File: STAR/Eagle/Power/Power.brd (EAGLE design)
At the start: 51 x 40.4 mm, 51 parts, among them J1 J30J-25, U1 LMR16020, U2 LMR16020, U3 LMR16020

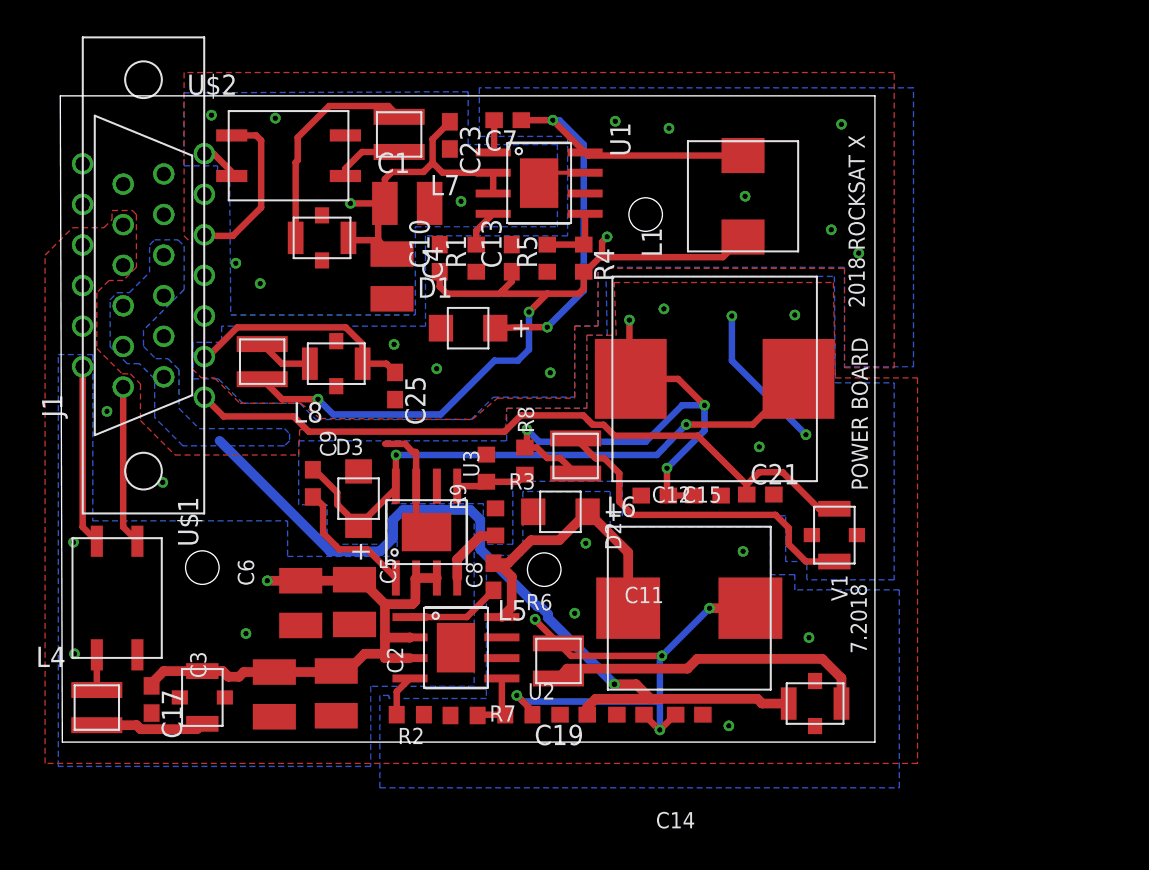
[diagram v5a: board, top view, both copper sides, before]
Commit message: Fixed Blaire's  nonsense on the power board. No longer shorting 3V3 to GSE_GND. The input names still make no sense
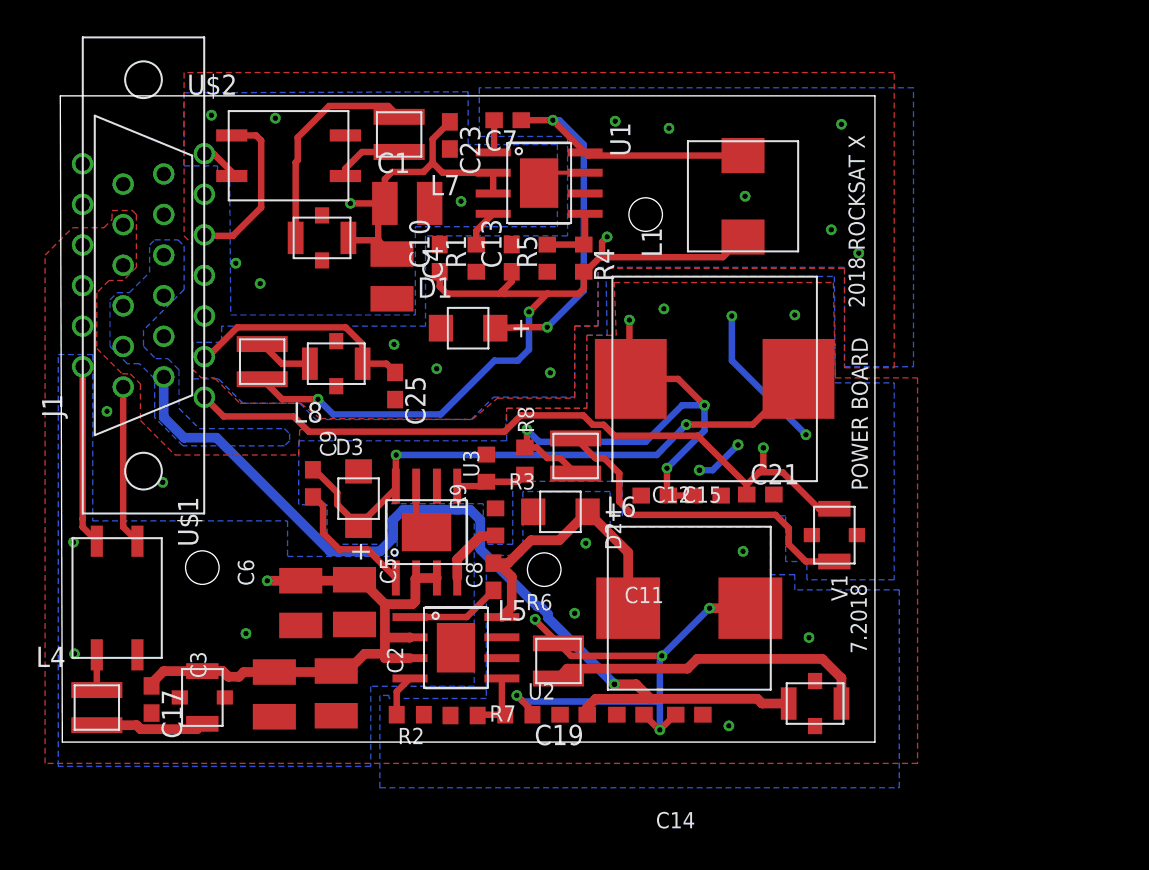
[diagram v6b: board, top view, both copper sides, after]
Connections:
- net EW renamed H
- net N$40 renamed L
- net N$42 renamed K
- net N$43 renamed J
- net N$44 renamed I
- net GSE_GND: now also U$4.P$4, U$4.P$5
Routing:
- net 5V_FILT: track 51.1 -> 57.8 mm
- net GSE_GND: track 16.8 -> 15.6 mm, vias 7 -> 8
- net 3V3_FILT: track 44.9 -> 46.1 mm, vias 0 -> 1
- net GSE_UFILT: track 11.9 -> 11.3 mm
- added copper zone on layer 16, net 3V3_FILT
- removed copper zone on layer 16, net GSE_GND
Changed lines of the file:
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@@
 <?xml version="1.0" encoding="utf-8"?>
 <!DOCTYPE eagle SYSTEM "eagle.dtd">
-<eagle version="7.6.0">
+<eagle version="9.1.0">
 <drawing>
 <settings>
 <setting alwaysvectorfont="no"/>
+<setting keepoldvectorfont="yes"/>
 <setting verticaltext="up"/>
 </settings>
@@
 <param name="dpMaxLengthDifference" value="10mm"/>
 <param name="dpGapFactor" value="2.5"/>
-<param name="checkGrid" value="0"/>
 <param name="checkAngle" value="0"/>
 <param name="checkFont" value="1"/>
 <param name="checkRestrict" value="1"/>
+<param name="checkStop" value="0"/>
+<param name="checkValues" value="0"/>
+<param name="checkNames" value="1"/>
+<param name="checkWireStubs" value="1"/>
+<param name="checkPolygonWidth" value="0"/>
 <param name="useDiameter" value="13"/>
 <param name="maxErrors" value="50"/>
@@
 <contactref element="U$1" pad="P$2"/>
 <contactref element="J1" pad="15"/>
-<wire x1="-4.191" y1="6.223" x2="-4.191" y2="5.588" width="0.4064" layer="1"/>
-<wire x1="-5.08" y1="17.145" x2="-5.08" y2="7.112" width="0.4064" layer="1"/>
-<wire x1="-5.08" y1="7.112" x2="-4.191" y2="6.223" width="0.4064" layer="1"/>
+<wire x1="-5.08" y1="17.145" x2="-5.08" y2="7.62" width="0.4064" layer="1"/>
+<wire x1="-5.08" y1="7.112" x2="-5.08" y2="7.62" width="0.4064" layer="1"/>
+<wire x1="-4.191" y1="6.223" x2="-5.08" y2="7.112" width="0.4064" layer="1"/>
 </signal>
 <signal name="GSE_FILT">
@@
 <wire x1="14.351" y1="6.4135" x2="13.5255" y2="5.588" width="0.6096" layer="16"/>
 <wire x1="13.5255" y1="5.588" x2="10.414" y2="5.588" width="0.6096" layer="16"/>
-<wire x1="10.414" y1="5.588" x2="3.4925" y2="12.5095" width="0.6096" layer="16"/>
 <wire x1="19.812" y1="5.715" x2="19.812" y2="7.5565" width="0.6096" layer="16"/>
 <via x="28.2054875" y="-2.7305" extent="1-16" drill="0.35"/>
 <wire x1="28.2054875" y1="-2.7305" x2="29.5656" y2="-2.7305" width="0.6096" layer="1"/>
 <wire x1="29.5656" y1="-2.7305" x2="30.48" y2="-3.6449" width="0.6096" layer="1"/>
+<wire x1="3.302" y1="12.7" x2="1.27" y2="12.7" width="0.6096" layer="16"/>
+<wire x1="1.27" y1="12.7" x2="0" y2="13.97" width="0.6096" layer="16"/>
+<wire x1="0" y1="13.97" x2="0" y2="16.51" width="0.6096" layer="16"/>
+<wire x1="10.414" y1="5.588" x2="3.302" y2="12.7" width="0.6096" layer="16"/>
 </signal>
 <signal name="3V3_FILT">
@@
 <wire x1="3.7465" y1="14.0335" x2="2.54" y2="15.24" width="0.4064" layer="1"/>
 <wire x1="22.352" y1="14.097" x2="26.26360625" y2="14.097" width="0.4064" layer="1"/>
-<wire x1="26.26360625" y1="14.097" x2="26.530303125" y2="13.830303125" width="0.4064" layer="1"/>
-<wire x1="26.530303125" y1="13.830303125" x2="26.83320625" y2="13.5274" width="0.4064" layer="1"/>
 <wire x1="33.4155" y1="12.827" x2="36.488" y2="9.7545" width="0.4064" layer="1"/>
-<wire x1="26.530303125" y1="13.830303125" x2="26.84800625" y2="13.5126" width="0.4064" layer="1"/>
-<wire x1="26.84800625" y1="13.5126" x2="27.52829375" y2="13.5126" width="0.4064" layer="1"/>
 <wire x1="27.52829375" y1="13.5126" x2="28.21389375" y2="12.827" width="0.4064" layer="1"/>
 <wire x1="28.21389375" y1="12.827" x2="33.4155" y2="12.827" width="0.4064" layer="1"/>
+<polygon width="0.4064" layer="16">
+<vertex x="45.72" y="3.81"/>
+<vertex x="40.259" y="3.81"/>
+<vertex x="40.259" y="4.953"/>
+<vertex x="38.9255" y="4.953"/>
+<vertex x="38.9255" y="7.8105"/>
+<vertex x="28.702" y="7.8105"/>
+<vertex x="28.702" y="9.9695"/>
+<vertex x="21.844" y="9.9695"/>
+<vertex x="21.844" y="6.0325"/>
+<vertex x="20.0025" y="6.0325"/>
+<vertex x="20.0025" y="8.5725"/>
+<vertex x="13.97" y="8.5725"/>
+<vertex x="13.97" y="6.0325"/>
+<vertex x="10.2235" y="6.0325"/>
+<vertex x="10.2235" y="8.509"/>
+<vertex x="8.4455" y="8.509"/>
+<vertex x="8.4455" y="12.5095"/>
+<vertex x="21.463" y="12.5095"/>
+<vertex x="21.463" y="14.5415"/>
+<vertex x="26.4795" y="14.5415"/>
+<vertex x="26.4795" y="19.1135"/>
+<vertex x="27.7495" y="19.1135"/>
+<vertex x="27.686" y="22.7965"/>
+<vertex x="41.9735" y="22.7965"/>
+<vertex x="42.037" y="16.129"/>
+<vertex x="45.72" y="16.129"/>
+</polygon>
+<via x="37.5285" y="12.065" extent="1-16" drill="0.35"/>
+<wire x1="37.5285" y1="12.065" x2="37.5285" y2="10.795" width="0.4064" layer="1"/>
+<wire x1="37.5285" y1="10.795" x2="37.2745" y2="10.541" width="0.4064" layer="1"/>
+<wire x1="26.26360625" y1="14.097" x2="26.84800625" y2="13.5126" width="0.4064" layer="1"/>
+<wire x1="26.84800625" y1="13.5126" x2="27.52829375" y2="13.5126" width="0.4064" layer="1"/>
 </signal>
 <signal name="N$29">
@@
 <wire x1="16.4465" y1="6.7945" x2="15.7965" y2="7.4445" width="0.4064" layer="1"/>
 <wire x1="15.7965" y1="7.4445" x2="15.7965" y2="9.6695" width="0.4064" layer="1"/>
-<wire x1="13.8557" y1="12.319" x2="15.113" y2="12.319" width="0.4064" layer="1"/>
-<wire x1="15.113" y1="12.319" x2="15.5575" y2="11.811" width="0.4064" layer="1"/>
-<wire x1="15.5575" y1="11.811" x2="15.748" y2="11.811" width="0.4064" layer="1"/>
-<wire x1="15.748" y1="11.811" x2="15.7965" y2="11.7625" width="0.4064" layer="1"/>
-<wire x1="15.7965" y1="11.7625" x2="15.7965" y2="9.6695" width="0.4064" layer="1"/>
 <contactref element="C6" pad="2"/>
 <contactref element="C3" pad="2"/>
@@
 <wire x1="35.56" y1="17.526" x2="40.1955" y2="12.8905" width="0.4064" layer="16"/>
 <via x="39.497" y="20.3835" extent="1-16" drill="0.3302" diameter="0.3302"/>
-<via x="37.2745" y="12.1285" extent="1-16" drill="0.3302" diameter="0.3302"/>
-<polygon width="0.4064" layer="16">
-<vertex x="45.72" y="3.81"/>
-<vertex x="40.259" y="3.81"/>
-<vertex x="40.259" y="4.953"/>
-<vertex x="38.9255" y="4.953"/>
-<vertex x="38.9255" y="7.8105"/>
-<vertex x="28.702" y="7.8105"/>
-<vertex x="28.702" y="9.9695"/>
-<vertex x="21.844" y="9.9695"/>
-<vertex x="21.844" y="6.0325"/>
-<vertex x="20.0025" y="6.0325"/>
-<vertex x="20.0025" y="8.5725"/>
-<vertex x="13.97" y="8.5725"/>
-<vertex x="13.97" y="6.0325"/>
-<vertex x="10.2235" y="6.0325"/>
-<vertex x="10.2235" y="8.509"/>
-<vertex x="8.4455" y="8.509"/>
-<vertex x="8.4455" y="12.5095"/>
-<vertex x="21.463" y="12.5095"/>
-<vertex x="21.463" y="14.5415"/>
-<vertex x="26.4795" y="14.5415"/>
-<vertex x="26.4795" y="19.1135"/>
-<vertex x="27.7495" y="19.1135"/>
-<vertex x="27.686" y="22.7965"/>
-<vertex x="41.9735" y="22.7965"/>
-<vertex x="42.037" y="16.129"/>
-<vertex x="45.72" y="16.129"/>
-</polygon>
-<wire x1="34.886" y1="9.0805" x2="38.188" y2="9.144" width="0" layer="19" extent="1-1"/>
+<contactref element="U$4" pad="P$4"/>
+<contactref element="U$4" pad="P$5"/>
+<via x="33.528" y="10.668" extent="1-16" drill="0.35"/>
+<via x="35.941" y="12.2555" extent="1-16" drill="0.35"/>
+<wire x1="33.528" y1="10.668" x2="34.3535" y2="10.668" width="0.4064" layer="16"/>
+<wire x1="34.3535" y1="10.668" x2="35.941" y2="12.2555" width="0.4064" layer="16"/>
 </signal>
 <signal name="TE_UFILT">
@@
 <contactref element="J1" pad="13"/>
 <wire x1="2.54" y1="30.48" x2="3.1115" y2="30.48" width="0.4064" layer="1"/>
-<wire x1="4.2545" y1="29.337" x2="3.1115" y2="30.48" width="0.4064" layer="1"/>
-<wire x1="4.2545" y1="29.337" x2="4.2545" y2="29.083" width="0" layer="19" extent="1-1"/>
-</signal>
-<signal name="N$40">
+<wire x1="3.1115" y1="30.48" x2="4.2545" y2="29.337" width="0.4064" layer="1"/>
+<wire x1="4.2545" y1="29.337" x2="4.2545" y2="29.083" width="0.4064" layer="1"/>
+</signal>
+<signal name="L">
 <contactref element="J1" pad="11"/>
 </signal>
-<signal name="N$42">
+<signal name="K">
 <contactref element="J1" pad="25"/>
 </signal>
-<signal name="N$43">
+<signal name="J">
 <contactref element="J1" pad="24"/>
 </signal>
-<signal name="N$44">
+<signal name="I">
 <contactref element="J1" pad="23"/>
 </signal>
@@
 <contactref element="J1" pad="10"/>
 </signal>
-<signal name="EW">
+<signal name="H">
 <contactref element="J1" pad="12"/>
 </signal>
 </signals>
+<mfgpreviewcolors>
+<mfgpreviewcolor name="soldermaskcolor" color="0xC8008000"/>
+<mfgpreviewcolor name="silkscreencolor" color="0xFFFEFEFE"/>
+<mfgpreviewcolor name="backgroundcolor" color="0xFF282828"/>
+<mfgpreviewcolor name="coppercolor" color="0xFFFFBF00"/>
+<mfgpreviewcolor name="substratecolor" color="0xFF786E46"/>
+</mfgpreviewcolors>
 </board>
 </drawing>

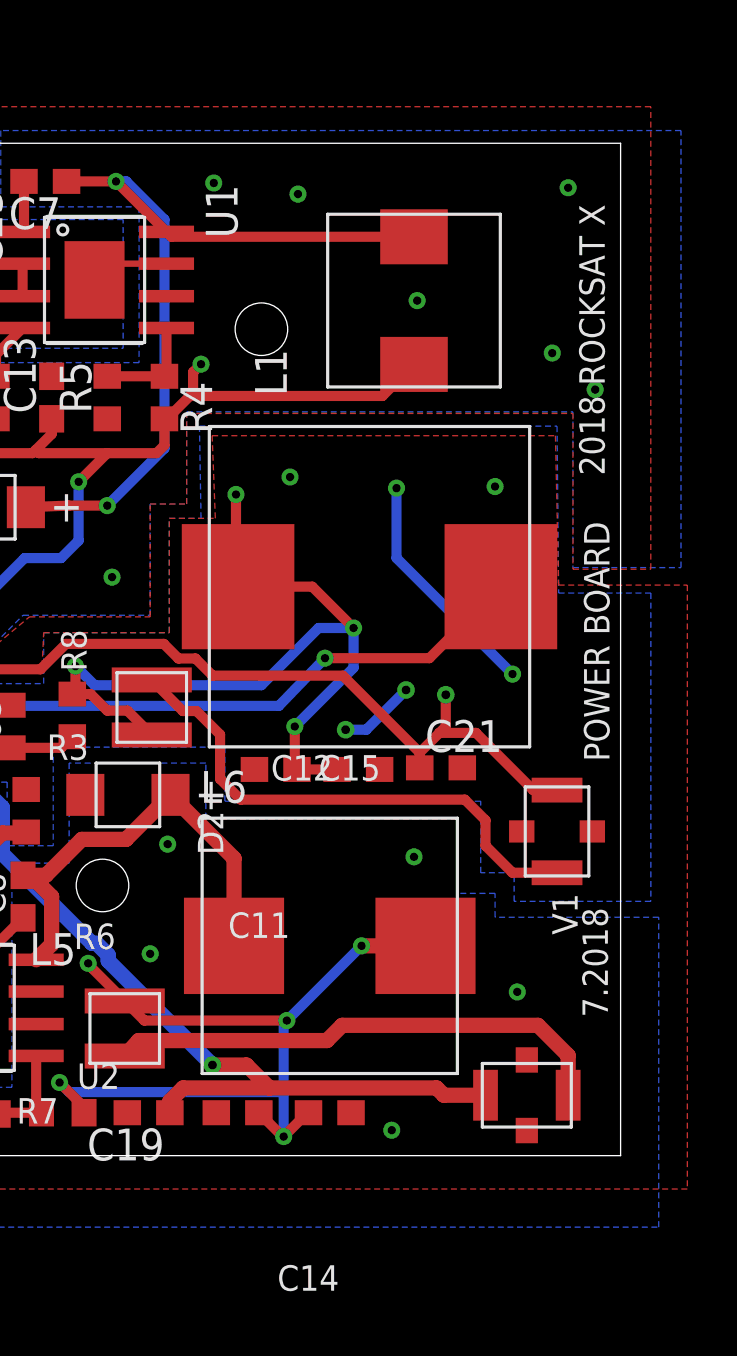
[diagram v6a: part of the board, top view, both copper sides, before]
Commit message: New inductors for the power board, changed the error message on the values script and added CBEs. Because who needs sleep
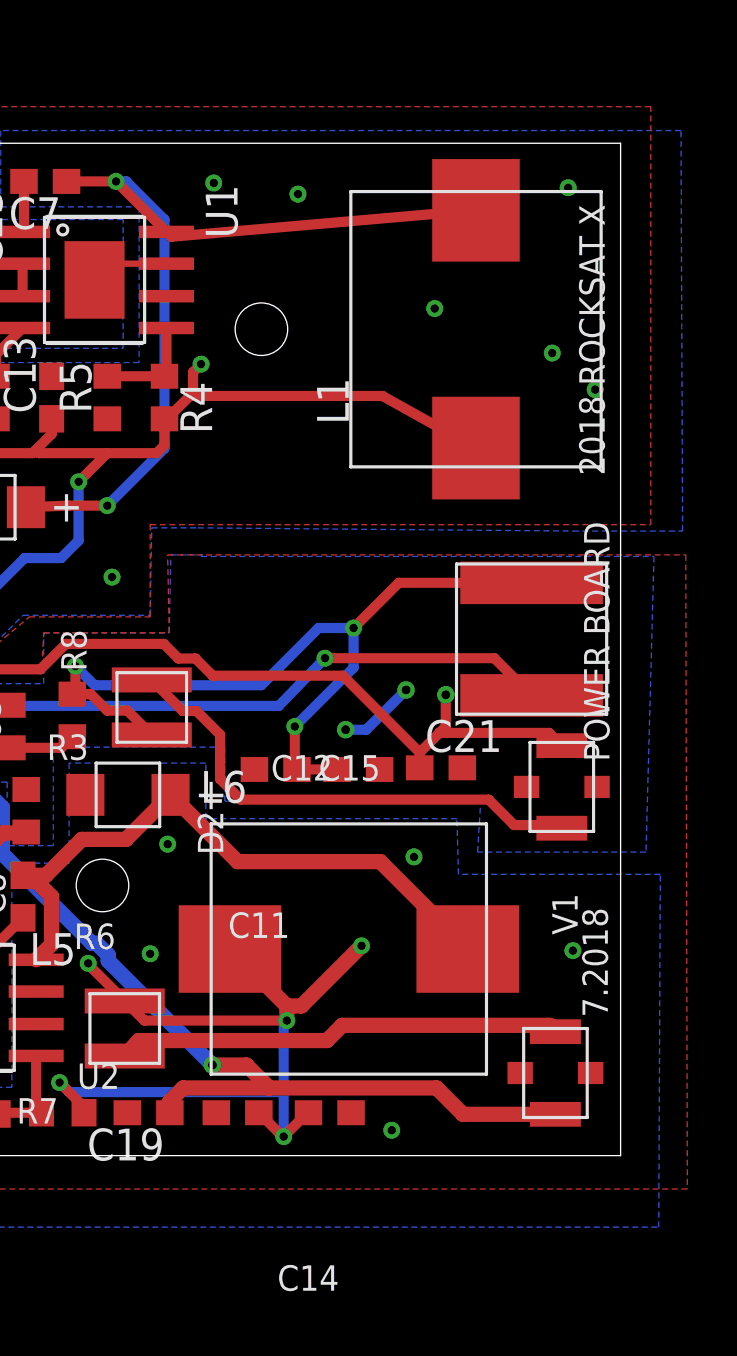
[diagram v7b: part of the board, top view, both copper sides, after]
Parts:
- L1: value 9.7u -> 30u; device Power:7050 -> Filtering:7050
- L2: value 5.5u -> 6.8u; device Filtering:1050 -> Filtering:7050
- L3: value 3.7u -> 30u; device Power:1365 -> Filtering:1365
- moved L3 6.81 mm to (41.0, 14.3), turned to 90 degrees
- moved L1 2.73 mm to (38.7, 26.7)
- moved U$5 1.79 mm to (42.2, 8.38)
- moved U$4 1.45 mm to (41.9, -3.05), turned to 270 degrees
- moved L2 0.77 mm to (33.7, 1.91)
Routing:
- net GSE_GND: track 15.6 -> 6.21 mm, vias 8 -> 4
- net N$5: track 18.6 -> 25.9 mm
- net 5V_FILT: track 57.8 -> 60.9 mm
- net N$14: track 33.0 -> 35.5 mm
- net +12V: track 48.5 -> 51.0 mm
- net N$32: track 20.3 -> 17.8 mm
- net +3V3: track 34.7 -> 33.5 mm, vias 4 -> 3
- net N$33: track 21.0 -> 19.9 mm
- net +5V: track 33.9 -> 34.9 mm
- net N$2: track 37.4 -> 38.1 mm
- net 3V3_FILT: track 46.1 -> 45.5 mm

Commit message: gerbers
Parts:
- removed C17, C19, C21, C23, C25: 1nF, resistor:C0603
- moved L7 12.4 mm to (6.29, 22.5)
- moved U$6 2.08 mm to (10.4, 23.2), turned to 90 degrees
- moved U$3 0.64 mm to (1.78, -3.49), turned to 270 degrees
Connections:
- new net N$38: U$1.P$3
- net 12V_FILT: no longer C25.1
- net 3V3_FILT: no longer C21.1
- net 5V_FILT: no longer C19.1
- net GND: no longer C23.2, C25.2
- net GSE_FILT: now also L4.P$2; no longer C17.1, U$3.P$2
- net GSE_GND: no longer C17.2, C19.2, C21.2, U$1.P$4
- net GSE_GND_IN: now also J1.15, U$1.P$2; no longer J1.14, U$1.P$1
- net GSE_UFILT: now also J1.14, U$1.P$1; no longer J1.15, U$1.P$2
- net N$28: now also U$3.P$2; no longer U$1.P$3
- net N$29: now also U$6.P$2; no longer L7.P$1
- net N$31: now also U$1.P$4; no longer L4.P$2
- net N$34: now also L7.P$1, U$6.P$3; no longer L7.P$2, U$6.P$2
- net TE_FILT: now also L7.P$2; no longer C23.1, U$6.P$3
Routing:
- net N$34: track 13.8 -> 4.10 mm
- net GSE_GND: track 6.21 -> 15.2 mm, vias 4 -> 5
- net GSE_FILT: track 35.1 -> 29.7 mm
- net N$28: track 2.20 -> 6.82 mm
- net N$31: track 6.85 -> 3.82 mm
- net TE_FILT: track 21.1 -> 18.3 mm
- net GSE_GND_IN: track 10.0 -> 11.3 mm
- net GSE_UFILT: track 11.3 -> 10.0 mm
- net 12V_FILT: track 14.6 -> 13.8 mm
- net 3V3_FILT: track 45.5 -> 44.9 mm
